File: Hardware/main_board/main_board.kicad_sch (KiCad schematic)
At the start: 0 parts

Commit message: sch: done cc1101
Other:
- sheet MCU ports: added BUTTON_BACK, BUTTON_DOWN, BUTTON_LEFT, BUTTON_OK, BUTTON_RIGHT, BUTTON_UP, CC1101_CS, CC1101_G0, DISPLAY_CS, DISPLAY_DI, DISPLAY_RST, I2C_SCL, I2C_SDA, IR_RX, IR_TX, NFC_CS, PA4, PA6, PA7, PB2, PB3, PC0, PC1, PC3, PERI_EN, RESET, RFID_CARRIER, RFID_OUT, RFID_PULL, RFID_RF_IN, RF_SW_0, SD_CD, SD_CS, SPEAKER, SPI_D_MISO, SPI_D_MOSI, SPI_D_SCK, SPI_R_MISO, SPI_R_MOSI, SPI_R_SCK, SWCLK, SWDIO, UART1_RX, UART1_TX, VIBRO, iBTN; removed none

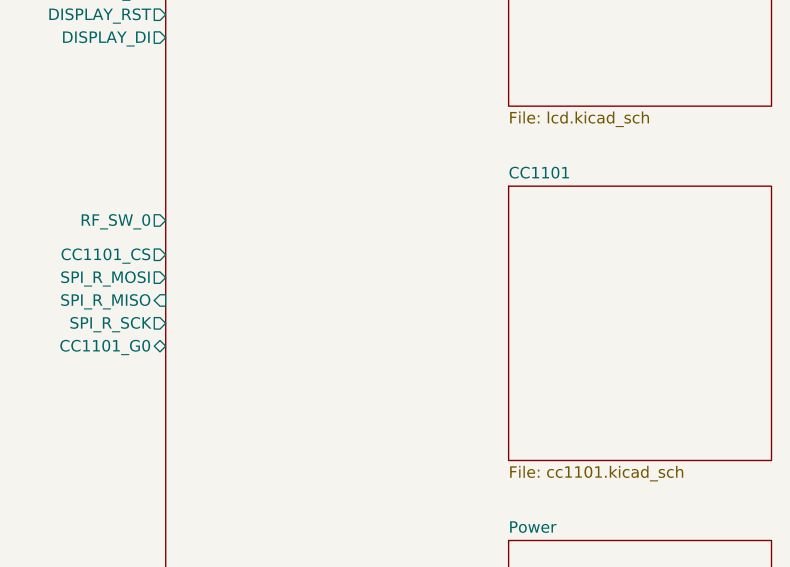
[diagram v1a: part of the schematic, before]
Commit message: sch: replace the SAW filter with a multilayer one
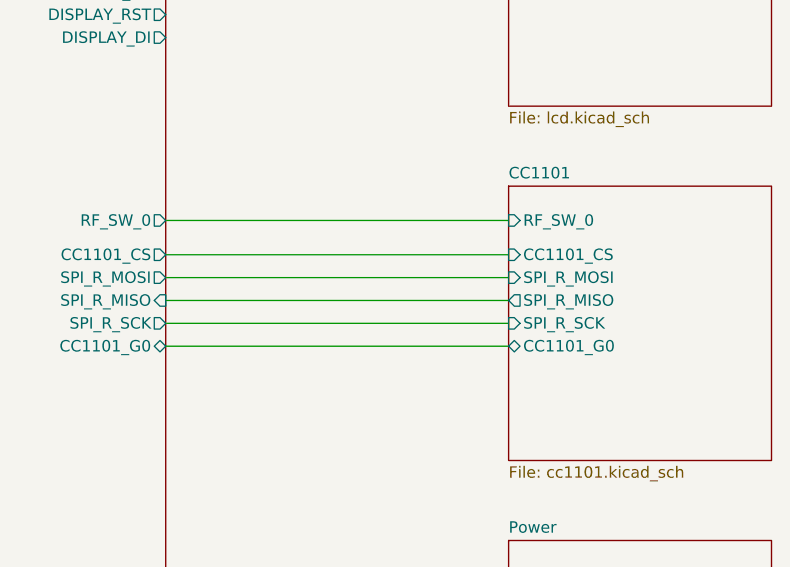
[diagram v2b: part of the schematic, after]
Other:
- sheet CC1101 ports: added CC1101_CS, CC1101_G0, RF_SW_0, SPI_R_MISO, SPI_R_MOSI, SPI_R_SCK; removed none
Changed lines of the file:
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@@
+	(wire
+		(pts
+			(xy 166.37 87.63) (xy 204.47 87.63)
+		)
+		(stroke
+			(width 0)
+			(type default)
+		)
+	)
 	(wire
 		(pts
@@
 	(wire
 		(pts
+			(xy 166.37 82.55) (xy 204.47 82.55)
+		)
+		(stroke
+			(width 0)
+			(type default)
+		)
+	)
+	(wire
+		(pts
 			(xy 166.37 114.3) (xy 204.47 114.3)
 		)
@@
 	(wire
 		(pts
+			(xy 166.37 80.01) (xy 204.47 80.01)
+		)
+		(stroke
+			(width 0)
+			(type default)
+		)
+	)
+	(wire
+		(pts
 			(xy 166.37 116.84) (xy 204.47 116.84)
 		)
@@
 	(wire
 		(pts
+			(xy 166.37 73.66) (xy 204.47 73.66)
+		)
+		(stroke
+			(width 0)
+			(type default)
+		)
+	)
+	(wire
+		(pts
+			(xy 166.37 85.09) (xy 204.47 85.09)
+		)
+		(stroke
+			(width 0)
+			(type default)
+		)
+	)
+	(wire
+		(pts
 			(xy 142.24 135.89) (xy 142.24 143.51)
+		)
+		(stroke
+			(width 0)
+			(type default)
+		)
+	)
+	(wire
+		(pts
+			(xy 166.37 77.47) (xy 204.47 77.47)
 		)
 		(stroke
@@
 			)
 		)
+		(pin "RF_SW_0" input
+			(at 204.47 73.66 180)
+			(effects
+				(font
+					(size 1.27 1.27)
+				)
+				(justify left)
+			)
+		)
+		(pin "CC1101_CS" input
+			(at 204.47 77.47 180)
+			(effects
+				(font
+					(size 1.27 1.27)
+				)
+				(justify left)
+			)
+		)
+		(pin "SPI_R_MISO" output
+			(at 204.47 82.55 180)
+			(effects
+				(font
+					(size 1.27 1.27)
+				)
+				(justify left)
+			)
+		)
+		(pin "SPI_R_MOSI" input
+			(at 204.47 80.01 180)
+			(effects
+				(font
+					(size 1.27 1.27)
+				)
+				(justify left)
+			)
+		)
+		(pin "SPI_R_SCK" input
+			(at 204.47 85.09 180)
+			(effects
+				(font
+					(size 1.27 1.27)
+				)
+				(justify left)
+			)
+		)
+		(pin "CC1101_G0" bidirectional
+			(at 204.47 87.63 180)
+			(effects
+				(font
+					(size 1.27 1.27)
+				)
+				(justify left)
+			)
+		)

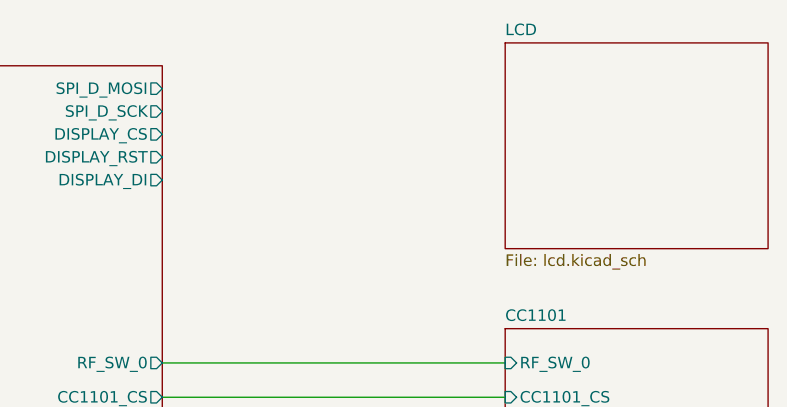
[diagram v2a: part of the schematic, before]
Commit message: sch: done LCD
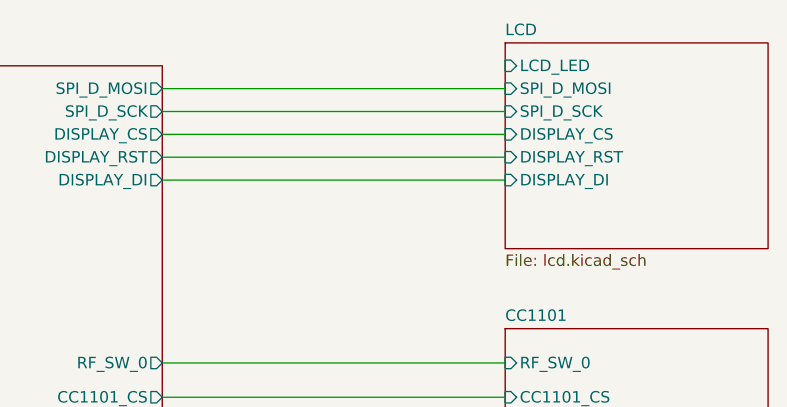
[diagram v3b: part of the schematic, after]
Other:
- sheet LCD ports: added DISPLAY_CS, DISPLAY_DI, DISPLAY_RST, LCD_LED, SPI_D_MOSI, SPI_D_SCK; removed none
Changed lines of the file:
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@@
+	(wire
+		(pts
+			(xy 166.37 45.72) (xy 204.47 45.72)
+		)
+		(stroke
+			(width 0)
+			(type default)
+		)
+	)
 	(wire
 		(pts
@@
 	(wire
 		(pts
+			(xy 166.37 48.26) (xy 204.47 48.26)
+		)
+		(stroke
+			(width 0)
+			(type default)
+		)
+	)
+	(wire
+		(pts
 			(xy 186.69 143.51) (xy 186.69 124.46)
 		)
@@
 	(wire
 		(pts
+			(xy 166.37 53.34) (xy 204.47 53.34)
+		)
+		(stroke
+			(width 0)
+			(type default)
+		)
+	)
+	(wire
+		(pts
+			(xy 166.37 43.18) (xy 204.47 43.18)
+		)
+		(stroke
+			(width 0)
+			(type default)
+		)
+	)
+	(wire
+		(pts
 			(xy 166.37 85.09) (xy 204.47 85.09)
 		)
@@
 		(pts
 			(xy 166.37 77.47) (xy 204.47 77.47)
+		)
+		(stroke
+			(width 0)
+			(type default)
+		)
+	)
+	(wire
+		(pts
+			(xy 166.37 50.8) (xy 204.47 50.8)
 		)
 		(stroke
@@
 			)
 		)
+		(pin "LCD_LED" input
+			(at 204.47 40.64 180)
+			(effects
+				(font
+					(size 1.27 1.27)
+				)
+				(justify left)
+			)
+		)
+		(pin "DISPLAY_RST" input
+			(at 204.47 50.8 180)
+			(effects
+				(font
+					(size 1.27 1.27)
+				)
+				(justify left)
+			)
+		)
+		(pin "DISPLAY_CS" input
+			(at 204.47 48.26 180)
+			(effects
+				(font
+					(size 1.27 1.27)
+				)
+				(justify left)
+			)
+		)
+		(pin "DISPLAY_DI" input
+			(at 204.47 53.34 180)
+			(effects
+				(font
+					(size 1.27 1.27)
+				)
+				(justify left)
+			)
+		)
+		(pin "SPI_D_MOSI" input
+			(at 204.47 43.18 180)
+			(effects
+				(font
+					(size 1.27 1.27)
+				)
+				(justify left)
+			)
+		)
+		(pin "SPI_D_SCK" input
+			(at 204.47 45.72 180)
+			(effects
+				(font
+					(size 1.27 1.27)
+				)
+				(justify left)
+			)
+		)

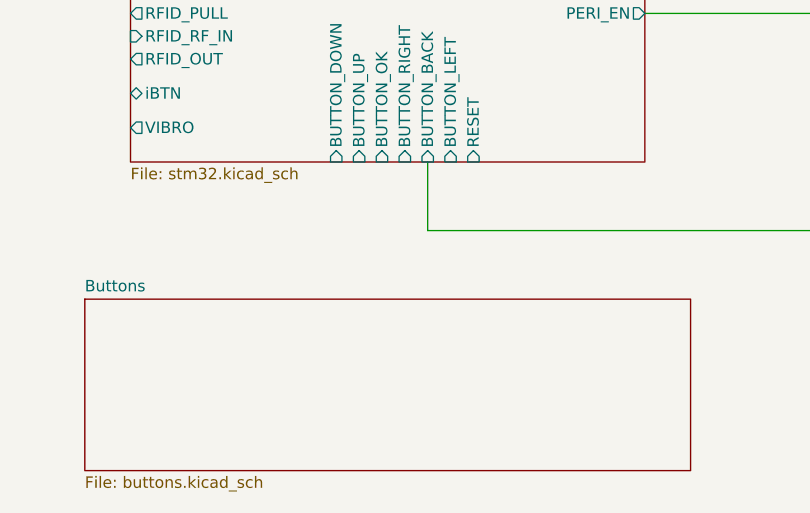
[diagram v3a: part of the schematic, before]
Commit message: sch: done buttons
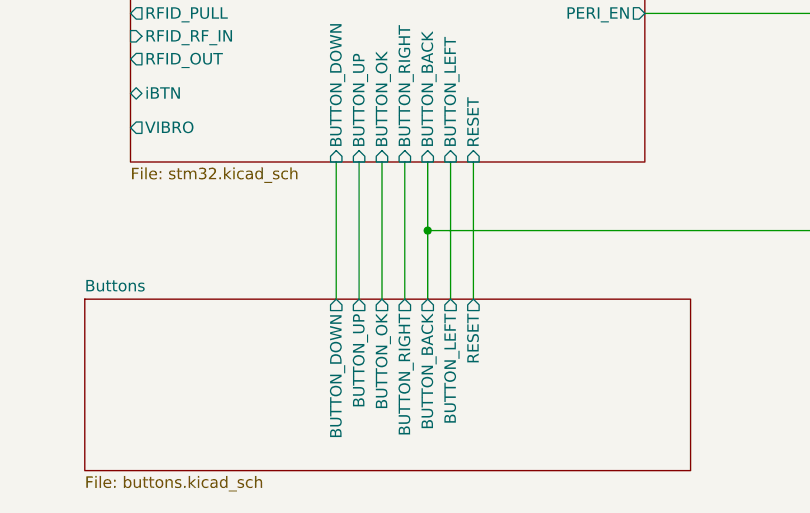
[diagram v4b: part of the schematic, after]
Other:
- sheet Buttons ports: added BUTTON_BACK, BUTTON_DOWN, BUTTON_LEFT, BUTTON_OK, BUTTON_RIGHT, BUTTON_UP, RESET; removed none
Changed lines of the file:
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@@
 	(generator_version "8.0")
 	(paper "A4")
+	(junction
+		(at 142.24 143.51)
+		(diameter 0)
+		(color 0 0 0 0)
+	)
+	(wire
+		(pts
+			(xy 132.08 135.89) (xy 132.08 151.13)
+		)
+		(stroke
+			(width 0)
+			(type default)
+		)
+	)
 	(wire
 		(pts
@@
 	(wire
 		(pts
+			(xy 139.7 135.89) (xy 139.7 151.13)
+		)
+		(stroke
+			(width 0)
+			(type default)
+		)
+	)
+	(wire
+		(pts
 			(xy 166.37 116.84) (xy 204.47 116.84)
 		)
@@
 	(wire
 		(pts
+			(xy 144.78 135.89) (xy 144.78 151.13)
+		)
+		(stroke
+			(width 0)
+			(type default)
+		)
+	)
+	(wire
+		(pts
 			(xy 186.69 124.46) (xy 204.47 124.46)
 		)
@@
 	(wire
 		(pts
+			(xy 134.62 135.89) (xy 134.62 151.13)
+		)
+		(stroke
+			(width 0)
+			(type default)
+		)
+	)
+	(wire
+		(pts
+			(xy 137.16 135.89) (xy 137.16 151.13)
+		)
+		(stroke
+			(width 0)
+			(type default)
+		)
+	)
+	(wire
+		(pts
+			(xy 142.24 143.51) (xy 142.24 151.13)
+		)
+		(stroke
+			(width 0)
+			(type default)
+		)
+	)
+	(wire
+		(pts
 			(xy 166.37 48.26) (xy 204.47 48.26)
 		)
@@
 		(pts
 			(xy 166.37 53.34) (xy 204.47 53.34)
+		)
+		(stroke
+			(width 0)
+			(type default)
+		)
+	)
+	(wire
+		(pts
+			(xy 147.32 135.89) (xy 147.32 151.13)
 		)
 		(stroke
@@
 			)
 		)
+		(pin "BUTTON_BACK" output
+			(at 142.24 151.13 90)
+			(effects
+				(font
+					(size 1.27 1.27)
+				)
+				(justify right)
+			)
+		)
+		(pin "BUTTON_OK" output
+			(at 137.16 151.13 90)
+			(effects
+				(font
+					(size 1.27 1.27)
+				)
+				(justify right)
+			)
+		)
+		(pin "BUTTON_LEFT" output
+			(at 144.78 151.13 90)
+			(effects
+				(font
+					(size 1.27 1.27)
+				)
+				(justify right)
+			)
+		)
+		(pin "BUTTON_DOWN" output
+			(at 132.08 151.13 90)
+			(effects
+				(font
+					(size 1.27 1.27)
+				)
+				(justify right)
+			)
+		)
+		(pin "BUTTON_UP" output
+			(at 134.62 151.13 90)
+			(effects
+				(font
+					(size 1.27 1.27)
+				)
+				(justify right)
+			)
+		)
+		(pin "BUTTON_RIGHT" output
+			(at 139.7 151.13 90)
+			(effects
+				(font
+					(size 1.27 1.27)
+				)
+				(justify right)
+			)
+		)
+		(pin "RESET" output
+			(at 147.32 151.13 90)
+			(effects
+				(font
+					(size 1.27 1.27)
+				)
+				(justify right)
+			)
+		)

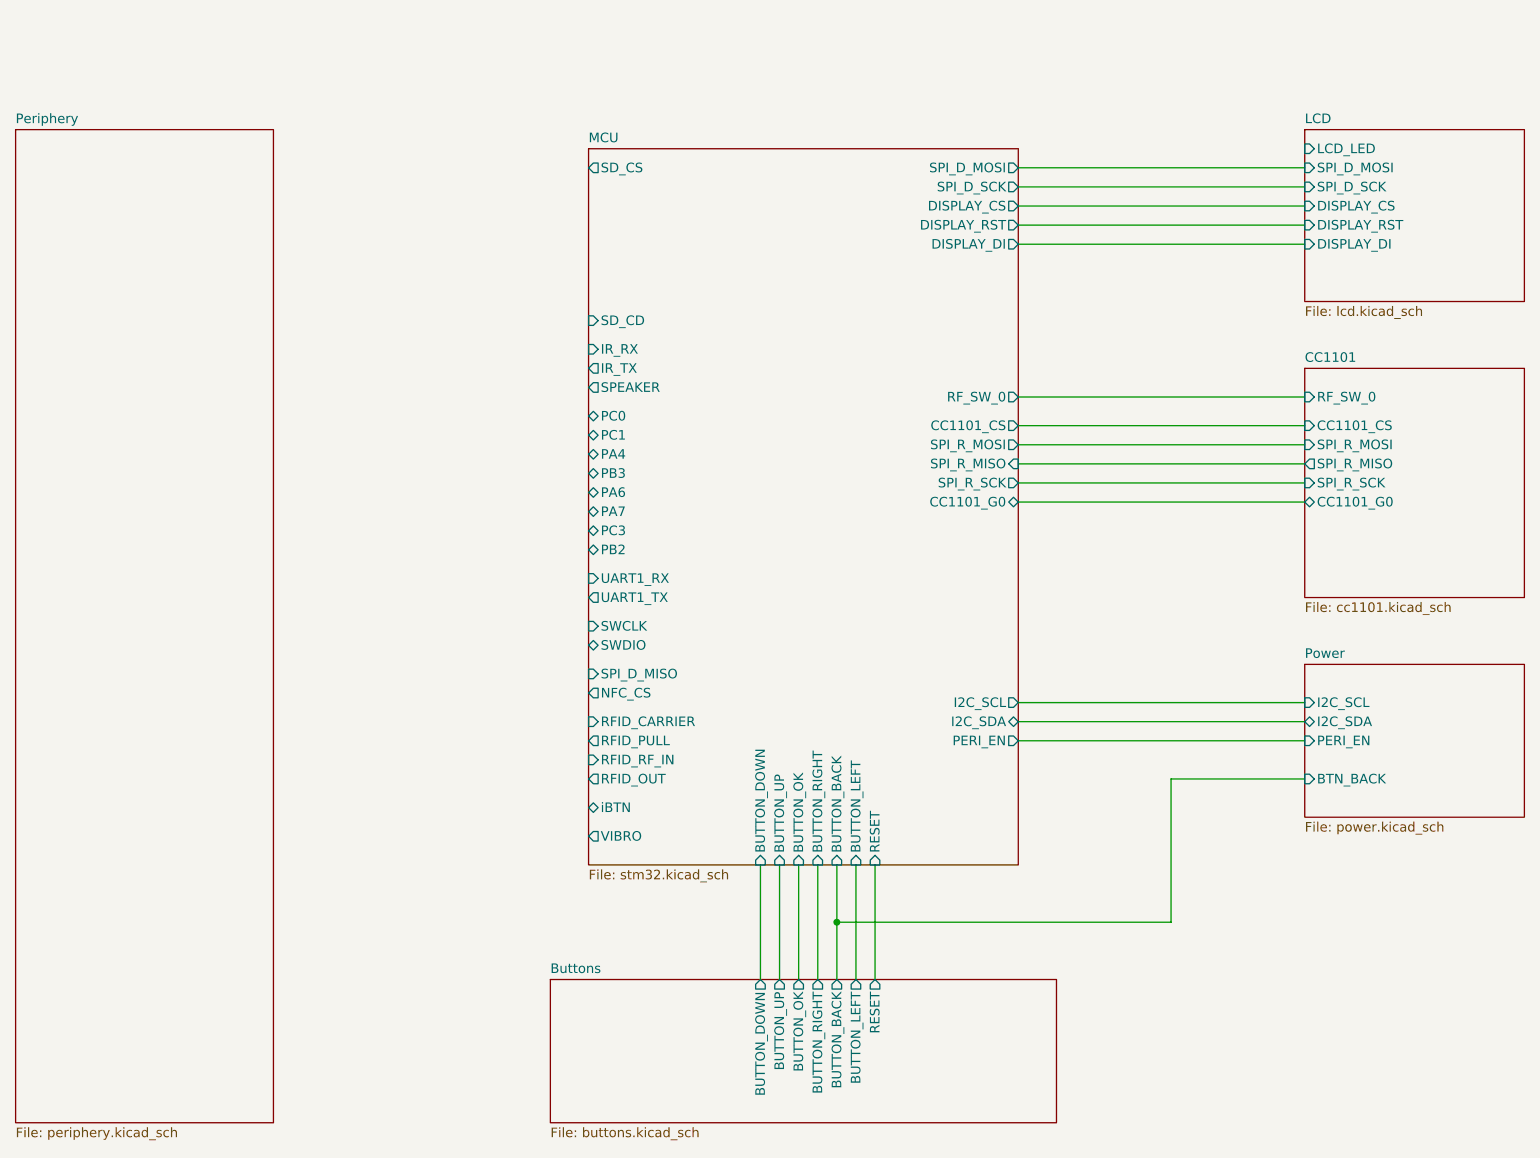
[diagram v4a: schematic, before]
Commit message: sch: done periphery
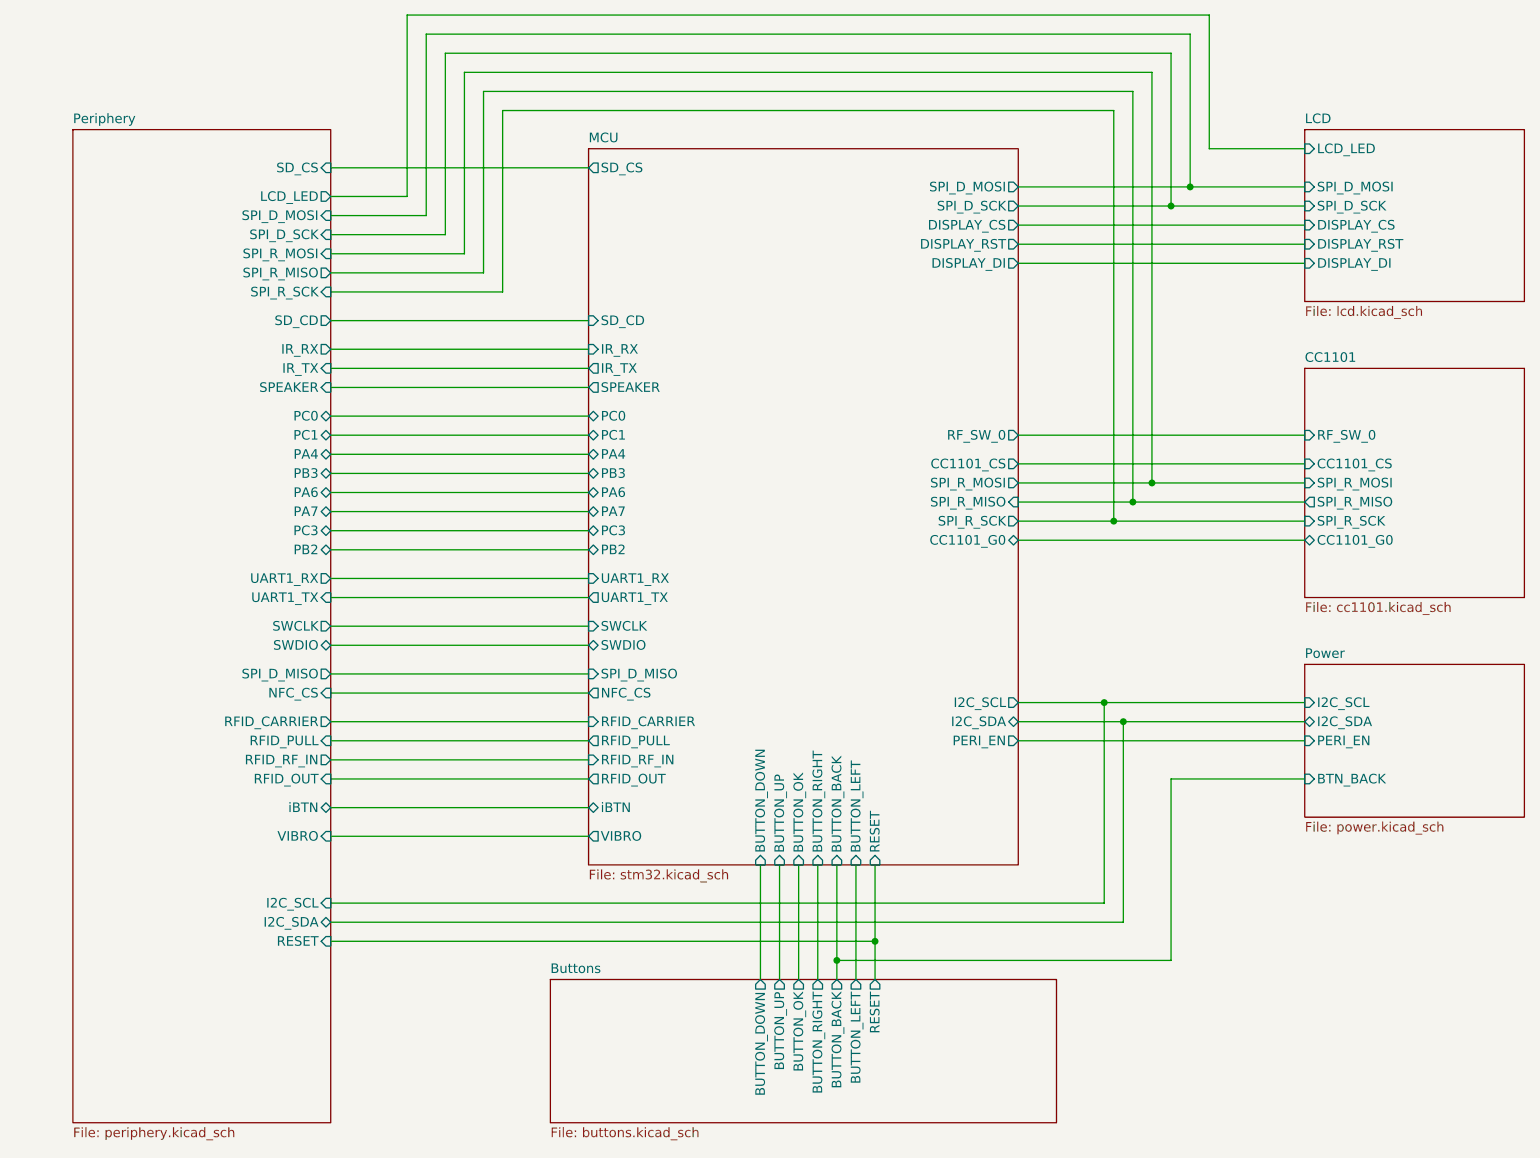
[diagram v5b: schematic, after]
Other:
- sheet Periphery ports: added I2C_SCL, I2C_SDA, IR_RX, IR_TX, LCD_LED, NFC_CS, PA4, PA6, PA7, PB2, PB3, PC0, PC1, PC3, RESET, RFID_CARRIER, RFID_OUT, RFID_PULL, RFID_RF_IN, SD_CD, SD_CS, SPEAKER, SPI_D_MISO, SPI_D_MOSI, SPI_D_SCK, SPI_R_MISO, SPI_R_MOSI, SPI_R_SCK, SWCLK, SWDIO, UART1_RX, UART1_TX, VIBRO, iBTN; removed none
